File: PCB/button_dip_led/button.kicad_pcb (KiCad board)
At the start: 2 copper layers, 40 x 46 mm, 27 parts, among them J2 Conn_01x03_Socket, J3 Lamp Seat, J4 RGB In, J5 RGB Out, J6 Gold Finger, J7 Gold Finger, SW2 Choc and IR Pair, U1 SS49E_SOT23

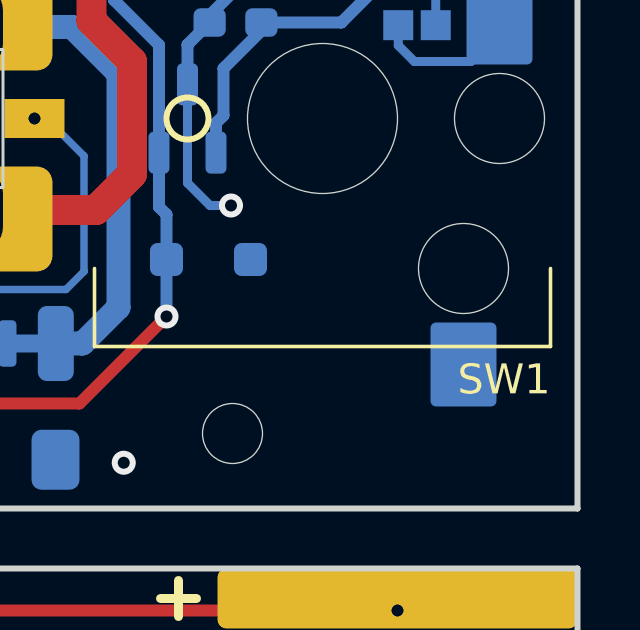
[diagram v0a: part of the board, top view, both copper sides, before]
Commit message: Fix SW1hotswap footprint
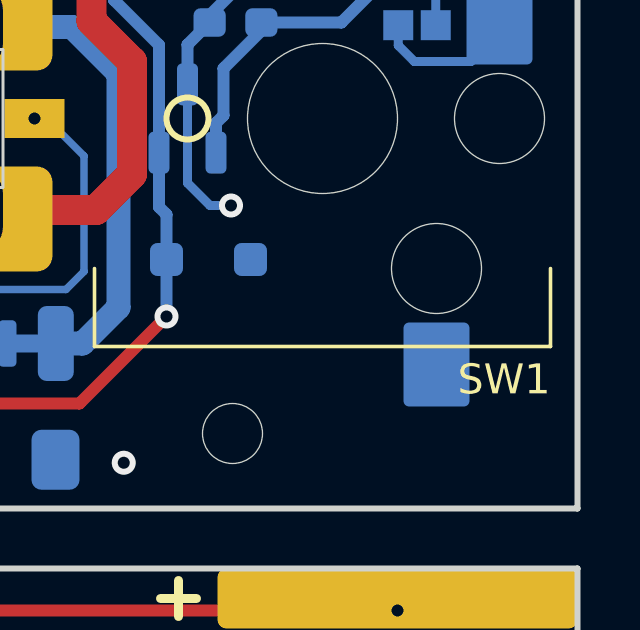
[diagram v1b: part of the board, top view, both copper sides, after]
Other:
- board text added: "Arcade Pico DIP Button v1.02"
- board text removed: "Arcade Pico Button v1.01"
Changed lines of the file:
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@@
 		)
 		(pad "" np_thru_hole circle
-			(at 5 -4.7 270)
+			(at 5 -3.8 270)
 			(size 3 3)
 			(drill 3)
@@
 		)
 		(pad "2" smd roundrect
-			(at 8.2 -4.7 270)
+			(at 8.2 -3.8 270)
 			(size 2.8 2.2)
 			(layers "B.Cu" "B.Mask" "B.Paste")
@@
 	)
 	(gr_text "github.com/whowechina"
-		(at 88.175 62.75 0)
+		(at 111.99 66.97 0)
 		(layer "B.SilkS")
 		(effects
@@
 		)
 	)
-	(gr_text "Arcade Pico\nButton v1.01"
-		(at 89.2 66.275 0)
+	(gr_text "Arcade Pico DIP\nButton v1.02"
+		(at 80.79 65.56 0)
 		(layer "B.SilkS")
 		(effects
@@
 				(thickness 0.1)
 			)
-			(justify left bottom mirror)
+			(justify right bottom mirror)
 		)
 	)
@@
 	)
 	(zone
-		(net 16)
-		(net_name "Net-(SW2B-A)")
+		(net 14)
+		(net_name "Net-(JP3-B)")
 		(layer "B.Cu")
 		(name "$teardrop_padvia$")
 		(hatch none 0.1)
-		(priority 30003)
+		(priority 30000)
 		(attr
 			(teardrop
@@
 		(polygon
 			(pts
-				(xy 91.904638 51.2) (xy 91.904638 50.8) (xy 91.779432 50.106231) (xy 91.039 50.15) (xy 90.811227 50.697166)
+				(xy 87.24056 58.635928) (xy 87.028428 58.84806) (xy 87.260694 60.534517) (xy 88.500707 60.500707)
+				(xy 88.840657 59.308255)
 			)
 		)
 	)
 	(zone
-		(net 14)
-		(net_name "Net-(JP3-B)")
+		(net 16)
+		(net_name "Net-(SW2B-A)")
 		(layer "B.Cu")
 		(name "$teardrop_padvia$")
 		(hatch none 0.1)
-		(priority 30000)
+		(priority 30003)
 		(attr
 			(teardrop
@@
 		(polygon
 			(pts
-				(xy 87.24056 58.635928) (xy 87.028428 58.84806) (xy 87.260694 60.534517) (xy 88.500707 60.500707)
-				(xy 88.840657 59.308255)
+				(xy 91.904638 51.2) (xy 91.904638 50.8) (xy 91.779432 50.106231) (xy 91.039 50.15) (xy 90.811227 50.697166)
 			)
 		)
 	)
 	(zone
-		(net 14)
-		(net_name "Net-(JP3-B)")
+		(net 15)
+		(net_name "Net-(JP4-B)")
 		(layer "B.Cu")
 		(name "$teardrop_padvia$")
 		(hatch none 0.1)
-		(priority 30001)
+		(priority 30002)
 		(attr
 			(teardrop
@@
 		(polygon
 			(pts
-				(xy 89.90342 58.808712) (xy 89.691288 58.59658) (xy 88.118986 59.319068) (xy 88.499293 60.500707)
-				(xy 89.739306 60.491489)
+				(xy 92.041772 59.131071) (xy 91.758929 58.848228) (xy 90.809143 59.303039) (xy 91.039293 59.850707)
+				(xy 91.779432 59.888386)
 			)
 		)
 	)
 	(zone
-		(net 15)
-		(net_name "Net-(JP4-B)")
+		(net 14)
+		(net_name "Net-(JP3-B)")
 		(layer "B.Cu")
 		(name "$teardrop_padvia$")
 		(hatch none 0.1)
-		(priority 30002)
+		(priority 30001)
 		(attr
 			(teardrop
@@
 		(polygon
 			(pts
-				(xy 92.041772 59.131071) (xy 91.758929 58.848228) (xy 90.809143 59.303039) (xy 91.039293 59.850707)
-				(xy 91.779432 59.888386)
+				(xy 89.90342 58.808712) (xy 89.691288 58.59658) (xy 88.118986 59.319068) (xy 88.499293 60.500707)
+				(xy 89.739306 60.491489)
 			)
 		)
